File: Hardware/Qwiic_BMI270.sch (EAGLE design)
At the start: 17 parts, among them J1 QWIIC_RIGHT_ANGLE, J2 QWIIC_RIGHT_ANGLE

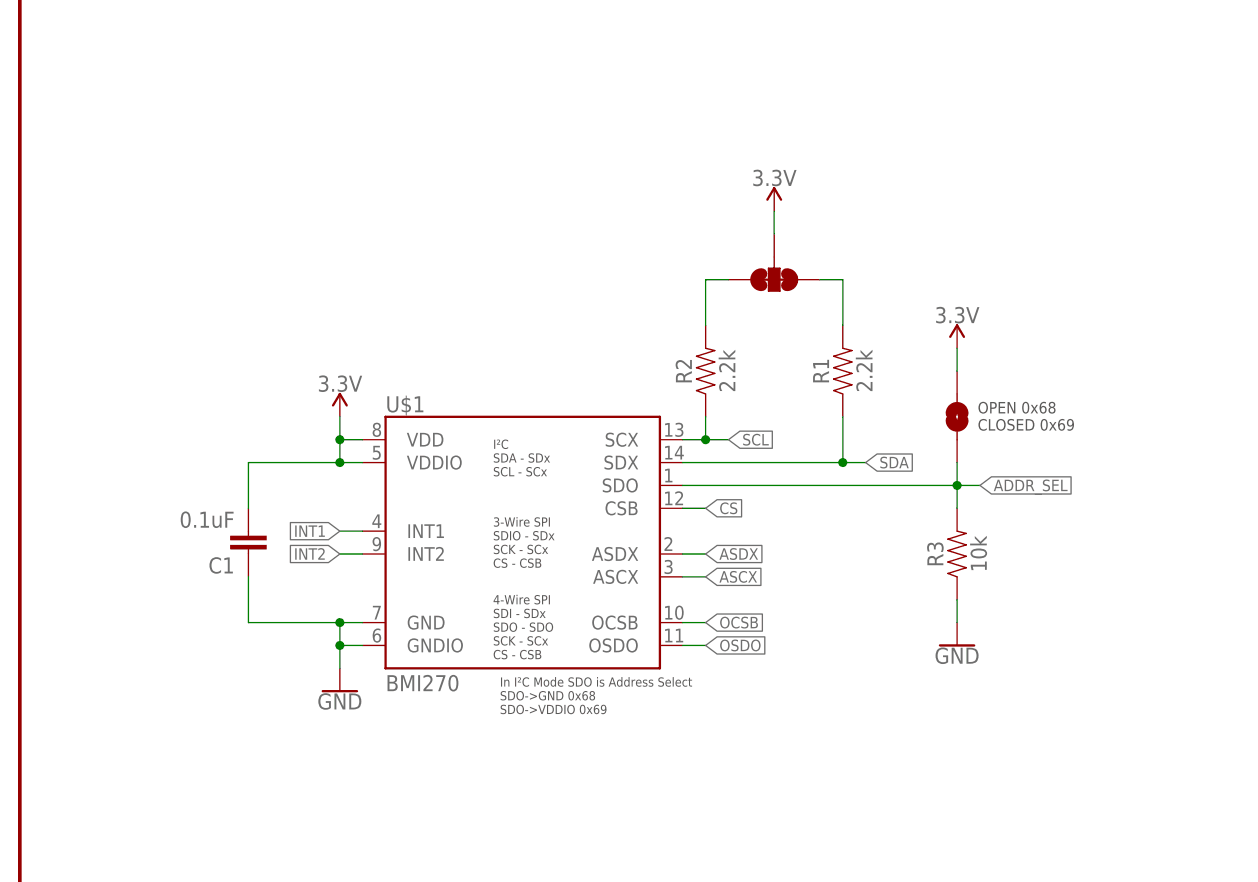
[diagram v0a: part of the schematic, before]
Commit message: Add BMI270 library file
Also replace part in sch/brd files with new library part
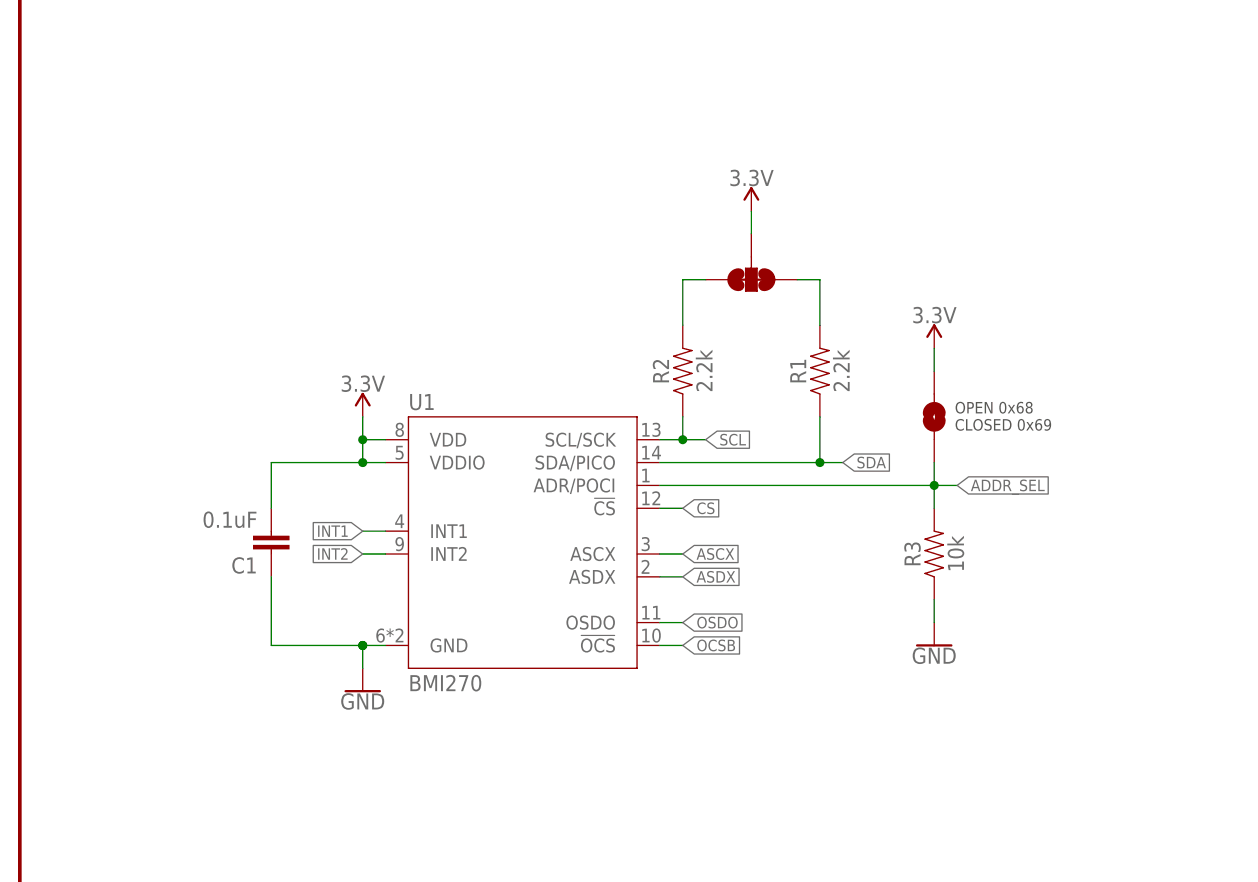
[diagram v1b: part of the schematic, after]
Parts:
- removed U$1: BMI270, SparkFun-Sensors:BMI270
- added U1: BMI270, BMI270:BMI270
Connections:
- net 3.3V: now also U1.VDD, U1.VDDIO; no longer U$1.VDD, U$1.VDDIO
- net ADDR_SEL: now also U1.ADR/POCI; no longer U$1.SDO
- net ASCX: now also U1.ASCX; no longer U$1.ASCX
- net ASDX: now also U1.ASDX; no longer U$1.ASDX
- net CS: now also U1.!CS!; no longer U$1.CSB
- net GND: now also U1.GND; no longer U$1.GND, U$1.GNDIO
- net INT1: now also U1.INT1; no longer U$1.INT1
- net INT2: now also U1.INT2; no longer U$1.INT2
- net OCSB: now also U1.!OCS!; no longer U$1.OCSB
- net OSDO: now also U1.OSDO; no longer U$1.OSDO
- net SCL: now also U1.SCL/SCK; no longer U$1.SCX
- net SDA: now also U1.SDA/PICO; no longer U$1.SDX
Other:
- moved on the sheet: C1, R1, R2, R3
